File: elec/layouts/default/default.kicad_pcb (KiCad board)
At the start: 2 copper layers, 46.5 x 25.5 mm, 10 parts

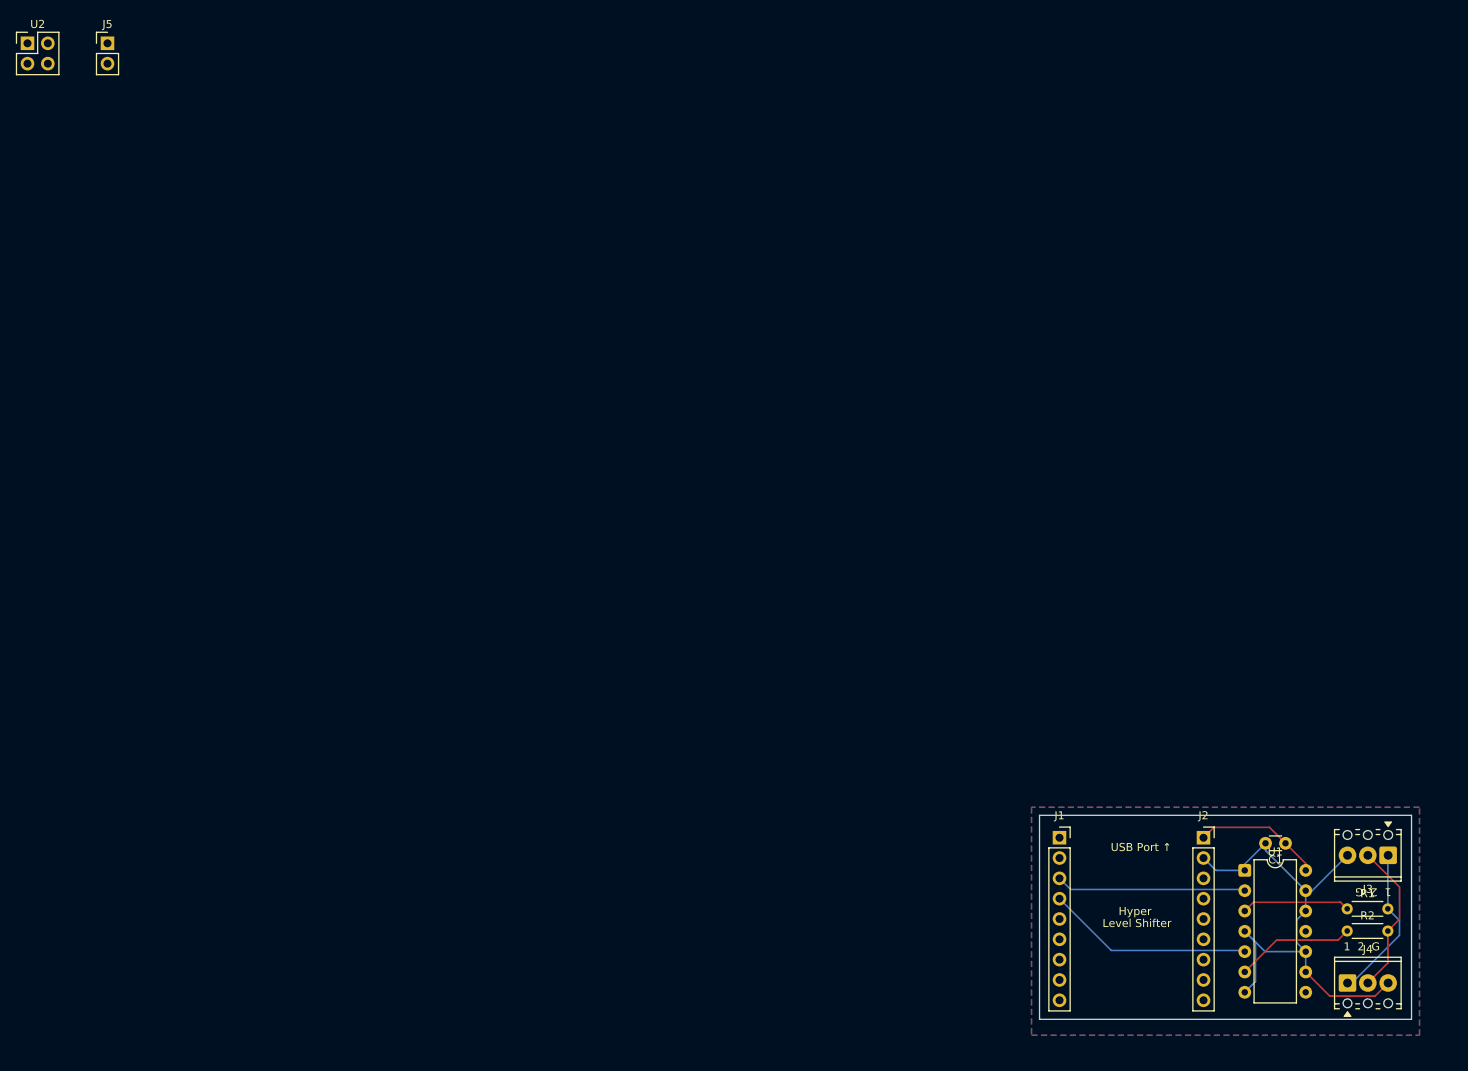
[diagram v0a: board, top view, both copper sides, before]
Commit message: Update footprints, fix power nets, update docs
- BuckModule_5V_Direct: correct pad positions to long edges (portrait orientation),
  mirror X axis for flat-face-down mounting
- PDTrigger_Direct: fix pad positions to non-USB-C end (bottom of board)
- level_shifter.ato: fix critical wiring bug — separate vcc_12v and vcc_5v nets
  (previously shorted IN+ to OUT+ through shared mcu.vcc_5v signal)
- CLAUDE.md: add layout TODO for next session, footprint verification notes
- README.md: rewrite for integrated-power variant with full BOM and assembly notes

Co-Authored-By: Claude Sonnet 4.6 <noreply@anthropic.com>
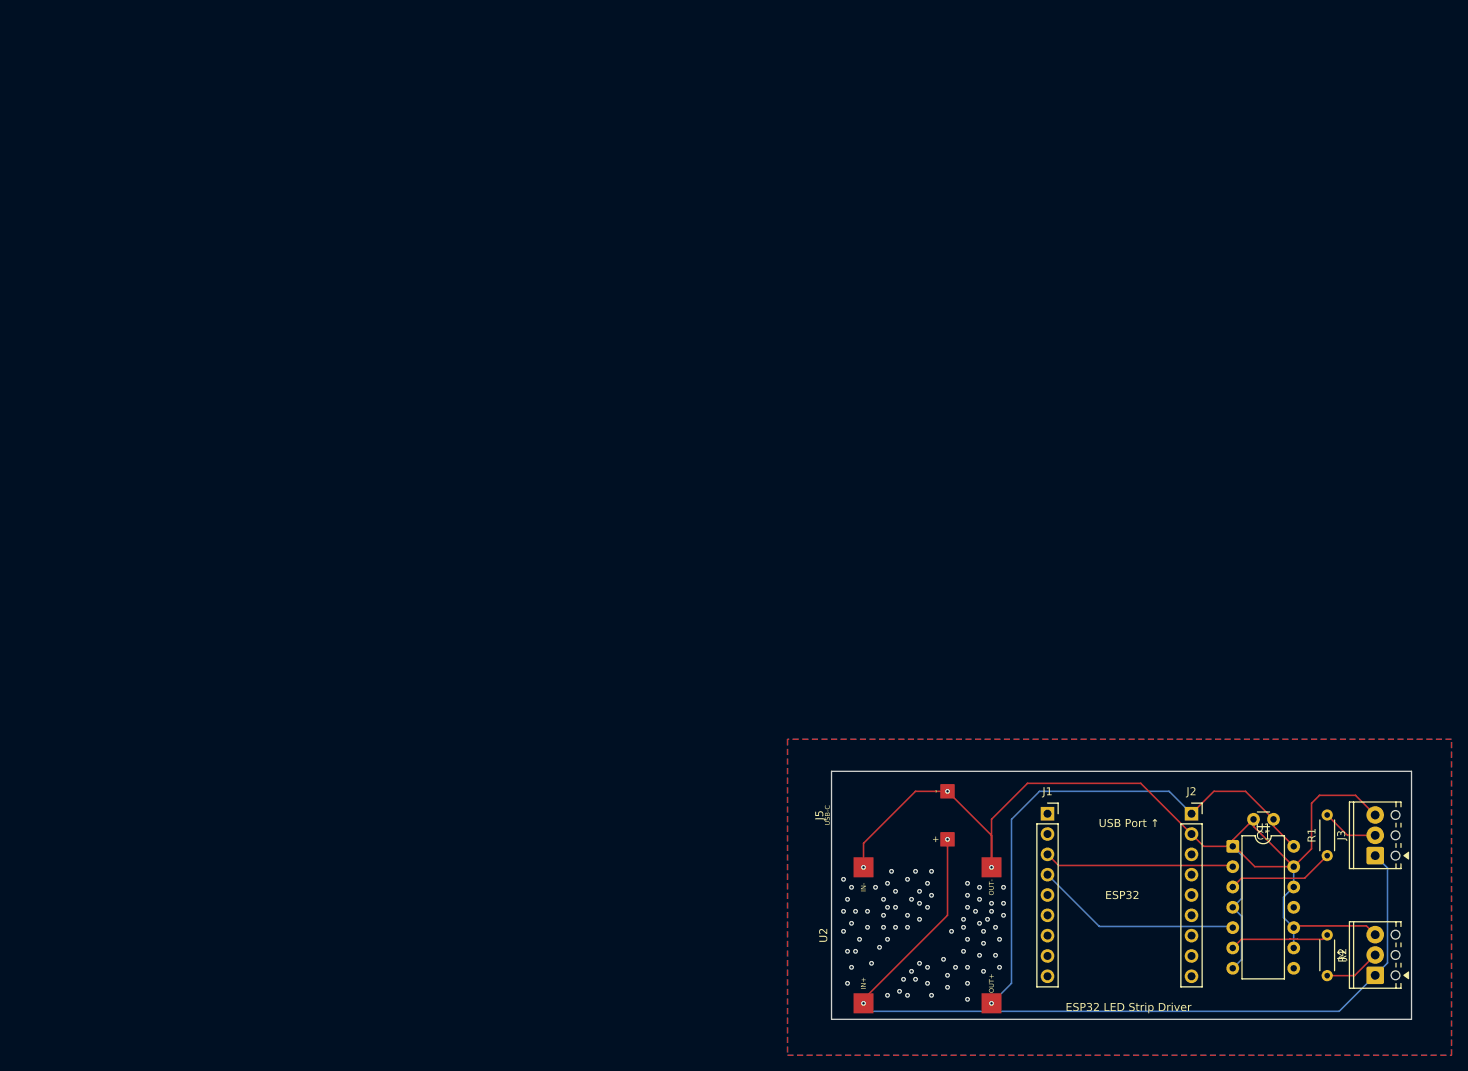
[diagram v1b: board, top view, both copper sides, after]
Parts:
- J5: footprint PowerConnector_1x2:PinHeader_1x02_P2.54mm_Vertical -> PowerConnector_1x2:PDTrigger_Direct
- U2: footprint BuckModule_5V:PinHeader_2x02_P2.54mm_Vertical -> BuckModule_5V:BuckModule_5V_Direct
- moved U2 158.4 mm to (112.5, 111.5), turned to 90 degrees
- moved J5 138.3 mm to (109.0, 96.5), turned to 90 degrees
- moved R1 7.11 mm to (162.5, 101.5), turned to 90 degrees
- moved J4 3.59 mm to (168.5, 116.5), turned to 90 degrees
- moved C1 3.35 mm to (155.8, 97.0)
- moved J1 3.35 mm to (127.5, 96.3)
- moved J2 3.35 mm to (145.5, 96.3)
- moved U1 3.35 mm to (150.7, 100.4)
- moved R2 2.55 mm to (162.5, 111.5), turned to -90 degrees
- moved J3 1.62 mm to (168.5, 101.5), turned to 90 degrees
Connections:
- C1 pad 1: 1 -> vcc_5v
- C1 pad 2: 2 -> gnd
- J1 pad 3: 2-1 -> 2
- J2 pad 1: 1 -> vcc_5v
- J2 pad 2: 2 -> gnd
- J3 pad 2: 2-2 -> 2-1
- J3 pad 3: 2 -> gnd
- J4 pad 2: 2-3 -> 2-2
- J4 pad 3: 2 -> gnd
- J5 pad 2: 2 -> gnd
- R1 pad 2: 2-2 -> 2-1
- R2 pad 2: 2-3 -> 2-2
- U1 pad 1: 2 -> gnd
- U1 pad 10: 2 -> gnd
- U1 pad 12: 2 -> gnd
- U1 pad 13: 2 -> gnd
- U1 pad 14: 1 -> vcc_5v
- U1 pad 2: 2-1 -> 2
- U1 pad 4: 2 -> gnd
- U1 pad 7: 2 -> gnd
- U1 pad 9: 2 -> gnd
- U2 pad 2: 2 -> gnd
- U2 pad 3: 1 -> vcc_5v
- U2 pad 4: 2 -> gnd
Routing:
- net gnd: track 0.00 -> 147.9 mm, vias 0 -> 85
- net 1: track 16.0 -> 107.3 mm, vias 0 -> 2
- net vcc_5v: track 0.00 -> 66.4 mm, vias 0 -> 1
- net 4: track 66.0 -> 0.00 mm
- net 2: track 0.00 -> 23.8 mm
- net 23: track 19.6 -> 0.00 mm
- net 2-3: track 19.2 -> 0.00 mm
- net 2-1: track 23.8 -> 7.05 mm
- net 2-2: track 0.00 -> 7.07 mm
- net 1-2: track 14.9 -> 12.5 mm
- added copper zone on B.Cu, net gnd
- added copper zone on F.Cu, net gnd
- removed copper zone on B.Cu, net 3
- removed copper zone on F.Cu, net 3
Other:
- board size 46.5 x 25.5 mm -> 72.5 x 31 mm
- board text added: "Buck Module"
- board text added: "ESP32"
- board text added: "ESP32 LED Strip Driver"
- board text added: "configure 12V before mounting"
- board text removed: "1 2 G"
- board text removed: "Hyper"
- board text removed: "Level Shifter"
